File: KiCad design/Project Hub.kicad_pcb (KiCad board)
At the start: 2 copper layers, 78 x 27.2 mm, 55 parts, among them M2 MountingHole_2.2mm_M2_Pad_Via, U1 GL850G-HHGXX(SSOP-28), Y1 12MHz

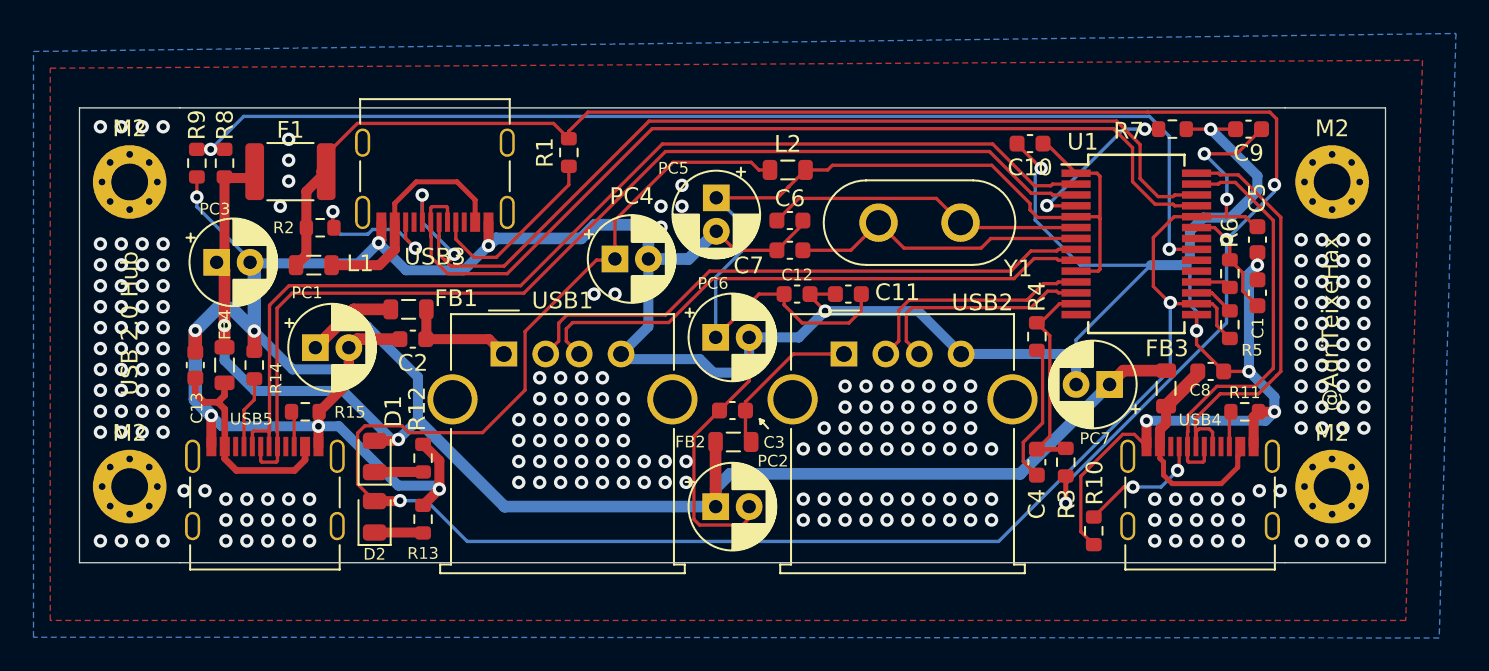
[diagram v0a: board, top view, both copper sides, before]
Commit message: fixed upstream port 5.1k resistors
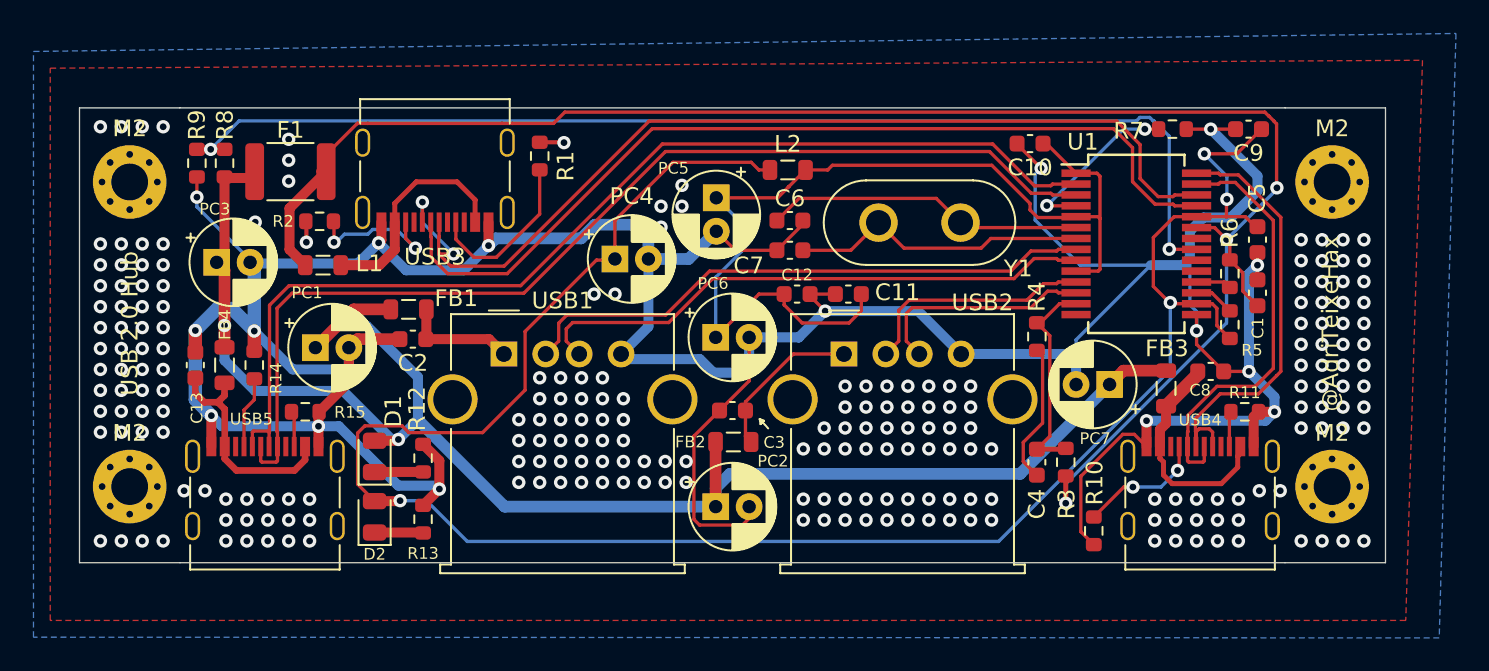
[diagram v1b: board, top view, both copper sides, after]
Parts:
- R1, R2: value 56K -> 5.1K
- R12: value 1K -> 10K
- R13: value 220R -> 10K
- moved R1 1.75 mm to (62.1, 84.9)
- moved L1 0.55 mm to (49.2, 91.4)
- moved R2 0.39 mm to (49.0, 88.8)
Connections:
- R1 pad 2: 5V -> GND
- R2 pad 2: 5V -> GND
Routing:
- net D0_N: track 57.7 -> 54.9 mm
- net GND: track 246.3 -> 249.0 mm, vias 244 -> 246
- net Net-(USB3-CC1): track 11.1 -> 10.2 mm
- net D0_P: track 61.2 -> 60.4 mm
- net Net-(USB3-CC2): track 9.39 -> 8.70 mm
- net Net-(L1-Pad1): track 14.1 -> 13.5 mm
